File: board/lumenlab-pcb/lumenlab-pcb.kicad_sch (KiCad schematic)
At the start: 19 parts, among them J1 Barrel_Jack, SW1 SW_SPST, U1 MP2338

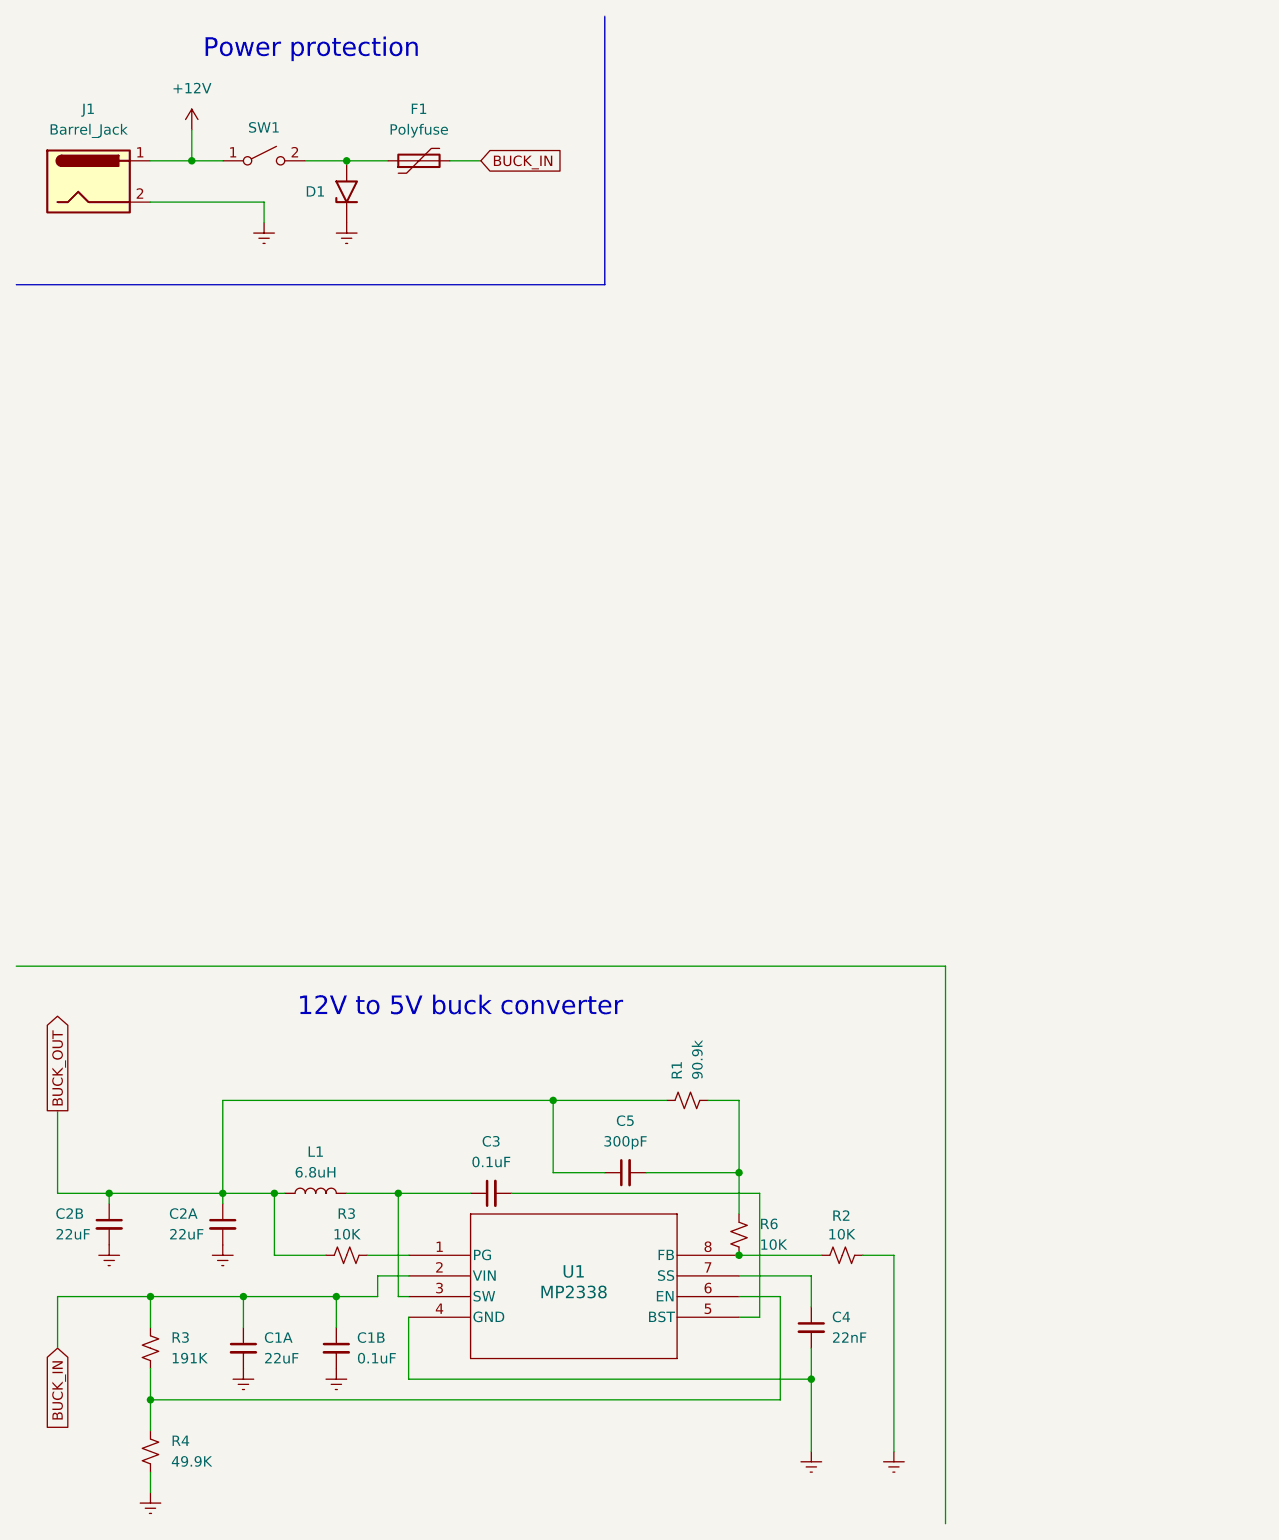
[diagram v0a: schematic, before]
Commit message: Add buck converter
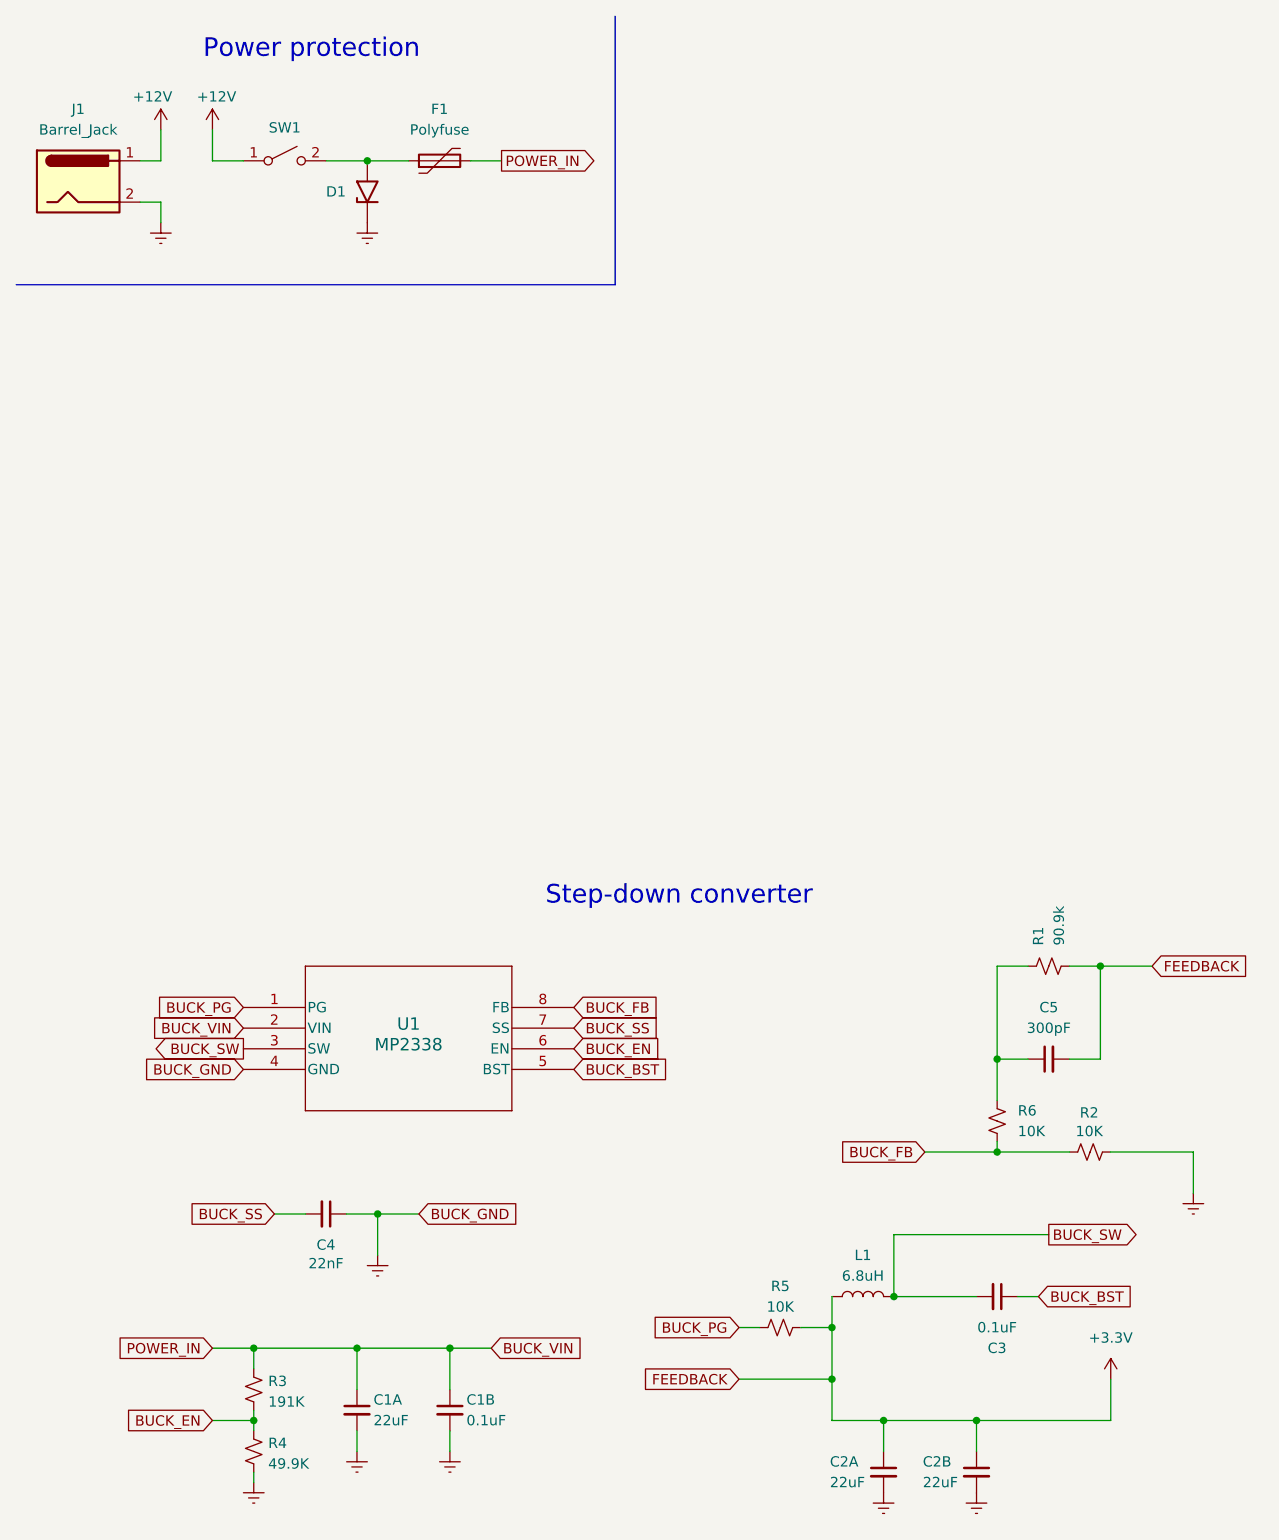
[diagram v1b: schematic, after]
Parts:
- removed R3: 10K, symbol Device:R_Small_US
- removed R3: 191K, symbol Device:R_Small_US
- added R3: 191K, symbol Device:R_Small_US
- added R5: 10K, symbol Device:R_Small_US
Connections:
- net Earth: now also C4.1; no longer C4.2
- net BUCK_PG: now reaches U1.1 (PG)
- net BUCK_PG: now also R5.1
- net +3.3V: now reaches C5.2, R1.2
- net +3.3V: now also C2A.1, C2B.1, L1.1, R5.2; no longer R6.1
- net BUCK_SW: now reaches L1.2, U1.3 (SW)
- net BUCK_SW: now also C3.2; no longer C3.1
- net BUCK_BST: now reaches U1.5 (BST)
- net BUCK_BST: now also C3.1; no longer C3.2
- net BUCK_EN: now reaches R4.1, U1.6 (EN)
- net BUCK_EN: now also R3.2
- net BUCK_SS: now reaches U1.7 (SS)
- net BUCK_SS: now also C4.2; no longer C4.1
- net BUCK_FB: now reaches R2.1, R6.2, U1.8 (FB)
- net BUCK_IN renamed BUCK_VIN
- net BUCK_VIN: now also R3.1
- removed net BUCK_OUT: C2A.1, C2B.1, C5.1, L1.1, R1.1
- new net: C5.1, R1.1, R6.1
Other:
- note added: "Step-down converter"
- note removed: "12V to 5V buck converter"
- moved on the sheet: C2A, C2B, C5, D1, F1, J1, R1, SW1, U1
